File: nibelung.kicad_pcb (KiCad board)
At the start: 2 copper layers, 35.6 x 32.5 mm, 57 parts, among them J1 JST_PH_01x03, J2 AudioJack3-TSW, J3 ScrewTerm_01x08_2.54mm, J4 ScrewTerm_01x08_2.54mm, J5 JST_SH_01x03, J6 JST_SH_01x03, SW1 PTS840 GK, SW2 PTS840 GK, U1 74HCT245, U2 LTC2850xS8, U3 MIC5219-5.0YM5, U4 ADP122AUJZ-3.3

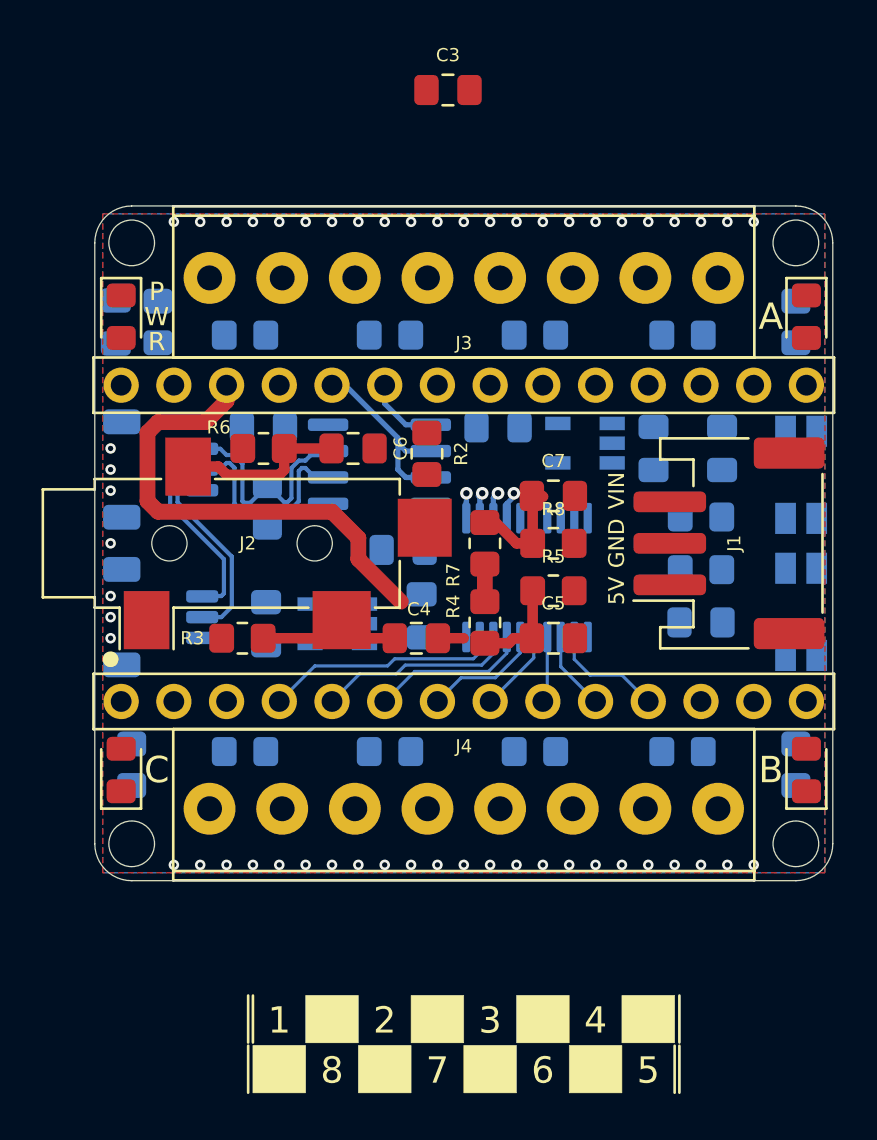
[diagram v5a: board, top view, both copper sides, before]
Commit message: Add properly colored STEP models
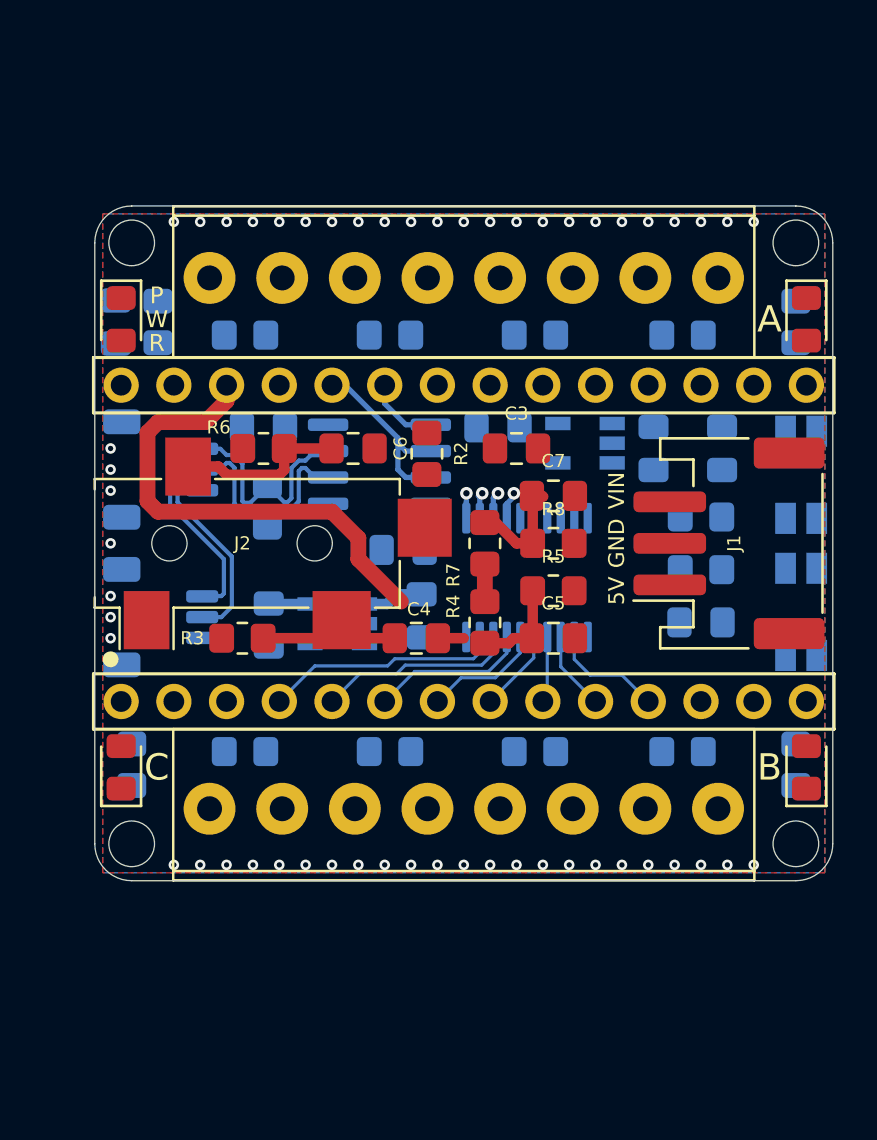
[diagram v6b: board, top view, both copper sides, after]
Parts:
- J2: footprint Connector_Audio:Jack_3.5mm_CUI_SJ-3524-SMT_Horizontal -> nibelung:Jack_CUI_SJ-3524
- R11: value 430 -> 470
- R12: value 680 -> 100
- R9: value 10k -> 1k
- moved C3 17.6 mm to (123.2, 97.0)
- moved C12 0.14 mm to (111.3, 105.5)
- moved D1 0.13 mm to (104.1, 90.8)
- moved D2 0.13 mm to (137.2, 90.8)
- moved D3 0.13 mm to (137.2, 112.4)
- moved D4 0.13 mm to (104.1, 112.4)
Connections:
- A1 pad 20: /AUD_DET -> /MIC_IN
- A1 pad 21: /INDA -> /AUD_DET
- A1 pad 25: Net-(A1-Pad25) -> /INDA
- H1 pad 1: GND -> (no net)
- H2 pad 1: GND -> (no net)
- H3 pad 1: GND -> (no net)
- H4 pad 1: GND -> (no net)
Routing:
- net +5V: track 0.00 -> 6.67 mm
- net +3V3: track 0.00 -> 2.00 mm
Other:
- board text removed: "1"
- board text removed: "2"
- board text removed: "3"
- board text removed: "4"
- board text removed: "5"
- board text removed: "6"
- board text removed: "7"
- board text removed: "8"

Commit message: Continue placement
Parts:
- moved C3 20.7 mm to (143.8, 94.6)
- moved C8 4.20 mm to (118.5, 106.0)
- moved C14 1.93 mm to (132.8, 107.2)
- moved C11 1.91 mm to (118.4, 103.2), turned to 90 degrees
- moved R2 1.17 mm to (119.8, 98.0), turned to 0 degrees
- moved R5 0.81 mm to (124.3, 104.4)
- moved C5 0.74 mm to (124.3, 106.6)
- moved C7 0.68 mm to (124.3, 99.6)
- moved R8 0.65 mm to (124.3, 101.7)
- moved R4 0.46 mm to (121.3, 105.7)
- moved R7 0.38 mm to (121.3, 101.6)
- moved C1 0.25 mm to (110.7, 96.0)
- moved U2 0.25 mm to (116.3, 97.8)
- moved R1 0.19 mm to (111.0, 99.8)
- moved C4 0.13 mm to (118.2, 106.2)
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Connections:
- A1 pad 12: Net-(A1-Pad12) -> /BTNA
- A1 pad 14: Net-(A1-Pad14) -> /BTNB
- R13 pad 1: /LED_OUT8 -> /LED_OUT1
- R14 pad 1: /LED_OUT7 -> /LED_OUT2
- R15 pad 1: /LED_OUT6 -> /LED_OUT3
- R16 pad 1: /LED_OUT5 -> /LED_OUT4
- R17 pad 1: /LED_OUT4 -> /LED_OUT5
- R18 pad 1: /LED_OUT3 -> /LED_OUT6
- R19 pad 1: /LED_OUT2 -> /LED_OUT7
- R20 pad 1: /LED_OUT1 -> /LED_OUT8
- U1 pad 1: +5V -> GND
- U1 pad 11: Net-(R20-Pad2) -> /LED8
- U1 pad 12: Net-(R19-Pad2) -> /LED7
- U1 pad 13: Net-(R18-Pad2) -> /LED6
- U1 pad 14: Net-(R17-Pad2) -> /LED5
- U1 pad 15: Net-(R16-Pad2) -> /LED4
- U1 pad 16: Net-(R15-Pad2) -> /LED3
- U1 pad 17: Net-(R14-Pad2) -> /LED2
- U1 pad 18: Net-(R13-Pad2) -> /LED1
- U1 pad 2: /LED8 -> Net-(R13-Pad2)
- U1 pad 3: /LED7 -> Net-(R14-Pad2)
- U1 pad 4: /LED6 -> Net-(R15-Pad2)
- U1 pad 5: /LED5 -> Net-(R16-Pad2)
- U1 pad 6: /LED4 -> Net-(R17-Pad2)
- U1 pad 7: /LED3 -> Net-(R18-Pad2)
- U1 pad 8: /LED2 -> Net-(R19-Pad2)
- U1 pad 9: /LED1 -> Net-(R20-Pad2)
- U2 pad 4: /DASHTX -> /DASH_TX
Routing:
- net +5V: track 6.67 -> 31.8 mm, vias 0 -> 1
- net +3V3: track 2.00 -> 21.9 mm
- net /AUD_DET: track 0.00 -> 9.17 mm, vias 0 -> 1
- net /AUD_R_ADC: track 5.02 -> 14.0 mm
- net +3V3A: track 25.1 -> 33.5 mm
- net /DASH_TX: track 0.00 -> 7.67 mm
- net Net-(R13-Pad2): track 0.00 -> 4.12 mm, vias 0 -> 1
- net Net-(R14-Pad2): track 0.00 -> 3.34 mm, vias 0 -> 1
- net GND: track 0.00 -> 1.96 mm, vias 53 -> 62
- net /AUD_R: track 8.21 -> 6.60 mm
- net Net-(R19-Pad2): track 1.58 -> 0.00 mm, vias 1 -> 0
- net Net-(R18-Pad2): track 1.54 -> 0.00 mm, vias 1 -> 0
- net /LED3: track 7.50 -> 8.94 mm
- net Net-(R17-Pad2): track 1.34 -> 0.00 mm, vias 1 -> 0
- net Net-(R20-Pad2): track 1.21 -> 0.00 mm, vias 1 -> 0
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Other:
- board text added: "1"
- board text added: "2"
- board text added: "3"
- board text added: "4"
- board text added: "5"
- board text added: "6"
- board text added: "7"
- board text added: "8"

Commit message: Finish layout
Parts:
- removed C13, C14: 0.1uF, Capacitor_SMD:C_0805_2012Metric_Pad1.18x1.45mm_HandSolder
- removed the C2 at (103.9, 90.9)
- removed the C3 at (143.8, 94.6)
- removed the C9 at (129.8, 97.0)
- removed R21, R22: 10k, Resistor_SMD:R_0805_2012Metric_Pad1.20x1.40mm_HandSolder
- added C1: 10uF, Capacitor_SMD:C_0805_2012Metric_Pad1.18x1.45mm_HandSolder, B.Cu at (129.9, 97.2)
- added G***: LOGO, nibelung:Logo_gdbg, B.Cu at (129.5, 106.6)
- added G***: LOGO, nibelung:Logo_Lion, B.Cu at (129.7, 102.6)
- added G***: LOGO, nibelung:Logo_Nibelung, F.Cu at (125.7, 96.5)
- added Q1: DMP3099L, Package_TO_SOT_SMD:SOT-23, B.Cu at (132.8, 97.0)
- added TP1: Pad, TestPoint:TestPoint_Pad_D1.5mm, B.Cu at (109.2, 91.6)
- added TP10: Pad, TestPoint:TestPoint_Pad_D1.5mm, B.Cu at (134.6, 111.6)
- added TP11: Pad, TestPoint:TestPoint_Pad_D1.5mm, B.Cu at (134.6, 91.6)
- added TP12: Pad, TestPoint:TestPoint_Pad_D1.5mm, B.Cu at (106.7, 111.6)
- added TP13: Pad, TestPoint:TestPoint_Pad_D1.5mm, B.Cu at (109.2, 111.6)
- added TP14: Pad, TestPoint:TestPoint_Pad_D1.5mm, B.Cu at (115.8, 102.1)
- added TP2: Pad, TestPoint:TestPoint_Pad_D1.5mm, B.Cu at (106.7, 91.6)
- added TP3: Pad, TestPoint:TestPoint_Pad_D1.5mm, B.Cu at (124.5, 91.6)
- added TP4: Pad, TestPoint:TestPoint_Pad_D1.5mm, B.Cu at (134.0, 104.5)
- added TP5: Pad, TestPoint:TestPoint_Pad_D1.5mm, B.Cu at (134.0, 106.8)
- added TP6: Pad, TestPoint:TestPoint_Pad_D1.5mm, B.Cu at (134.0, 102.2)
- added TP7: Pad, TestPoint:TestPoint_Pad_D1.5mm, B.Cu at (134.0, 99.9)
- added TP8: Pad, TestPoint:TestPoint_Pad_D1.5mm, B.Cu at (129.5, 111.6)
- added TP9: Pad, TestPoint:TestPoint_Pad_D1.5mm, B.Cu at (132.1, 111.6)
- D4: value BLUE -> BLU
- R8: value 47k -> 100k
- U4: value ADP122AUJZ-3.3 -> MIC5317-3.3YM5
- moved R17 27.2 mm to (112.8, 111.6)
- moved R20 25.7 mm to (126.1, 111.6)
- moved R18 21.2 mm to (117.2, 111.6)
- moved R19 20.6 mm to (121.7, 111.6), turned to 180 degrees
- moved R15 20.3 mm to (121.2, 91.6), turned to 0 degrees
- moved R13 20.2 mm to (112.5, 91.6), turned to 0 degrees
- moved R16 20.1 mm to (130.7, 91.6)
- moved R14 20.1 mm to (116.8, 91.6), turned to 0 degrees
- moved C8 2.05 mm to (125.3, 101.3), turned to 270 degrees
- moved R9 1.78 mm to (104.1, 90.9), turned to 270 degrees
- moved R5 1.63 mm to (123.3, 105.7), turned to 90 degrees
- moved C6 1.35 mm to (125.3, 105.7), turned to 90 degrees
- moved R8 1.09 mm to (123.3, 101.3), turned to 270 degrees
- moved R10 0.51 mm to (137.2, 90.9)
- moved R11 0.51 mm to (137.2, 112.3)
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- renumbered C8 to C10, C10 to C2, C11 to C3, C12 to C4, C4 to C5, C5 to C6, C6 to C7, C7 to C8, C1 to C9
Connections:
- net /DASH_RX renamed /DATA_RX
- net /DASH_TX renamed /DATA_TX
- net /DASH_TXEN renamed /DATA_TXEN
- J4 pad 2: /LED_OUT8 -> /LED_OUT5
- J4 pad 4: /LED_OUT7 -> /LED_OUT6
- J4 pad 6: /LED_OUT6 -> /LED_OUT7
- J4 pad 8: /LED_OUT5 -> /LED_OUT8
- U3 pad 1: VIN -> Net-(C1-Pad1)
- U3 pad 3: VIN -> Net-(C1-Pad1)
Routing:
- net +5V: track 31.8 -> 67.6 mm, vias 1 -> 4
- net /INDB: track 0.00 -> 32.4 mm
- net /INDA: track 0.00 -> 28.2 mm
- net Net-(R19-Pad2): track 0.00 -> 27.4 mm, vias 0 -> 2
- net Net-(R17-Pad2): track 0.00 -> 27.2 mm, vias 0 -> 2
- net Net-(R18-Pad2): track 0.00 -> 24.8 mm, vias 0 -> 2
- net Net-(R20-Pad2): track 0.00 -> 22.9 mm, vias 0 -> 2
- net /BTNA: track 0.00 -> 20.1 mm
- net /AUD_L_ADC: track 6.46 -> 24.7 mm
- net Net-(R15-Pad2): track 0.00 -> 16.8 mm, vias 0 -> 2
- net GND: track 1.96 -> 17.6 mm, vias 62 -> 54
- net Net-(R13-Pad2): track 4.12 -> 18.4 mm, vias 1 -> 2
- net Net-(R14-Pad2): track 3.34 -> 17.4 mm, vias 1 -> 2
- net Net-(R16-Pad2): track 0.00 -> 13.7 mm, vias 0 -> 2
- net /UART_TX: track 0.00 -> 13.6 mm
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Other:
- net class Audio added: clearance 0.254, trace_width 0.381, via_dia 0.762, via_drill 0.381
- net class Default: clearance 0.2032 -> 0.1524
- net class LED_Out added: clearance 0.2032, trace_width 0.254, via_dia 0.6096, via_drill 0.3048
- rule trace_clearance: 0.2032 -> 0.1524
- board text added: "0"
- board text added: "10"
- board text added: "11"
- board text added: "12"
- board text added: "13"
- board text added: "18"
- board text added: "3V3"
- board text added: "DATA"
- board text added: "DO NOT GO GENTLE"
- board text added: "LED Controller"
- board text added: "MIC"
- board text added: "RX"
- board text added: "SUBTRACT ECO2.USER LAYER FROM B.SILKS FOR INVERTED TEXT"
- board text added: "TX"
- board text added: "V"
- board text added: "v1.0"
- board text removed: "DASH"
